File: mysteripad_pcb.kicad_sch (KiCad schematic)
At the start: 74 parts, among them J1 PJ-320A, U1 ATmega328P-PU, Y1 Crystal

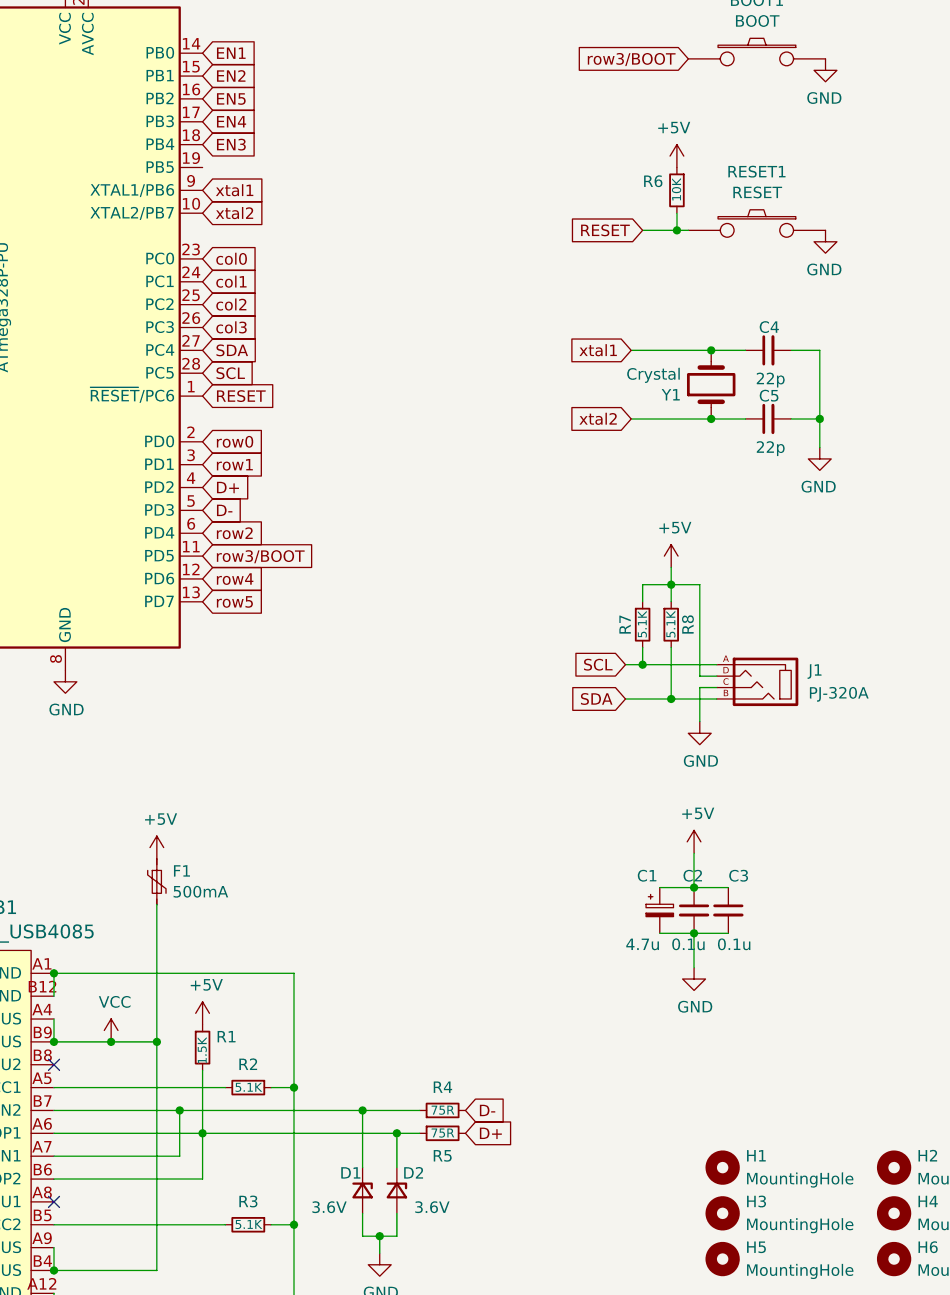
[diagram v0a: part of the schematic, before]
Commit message: Fix incorrect USB pullup; fix bottom mounting holes
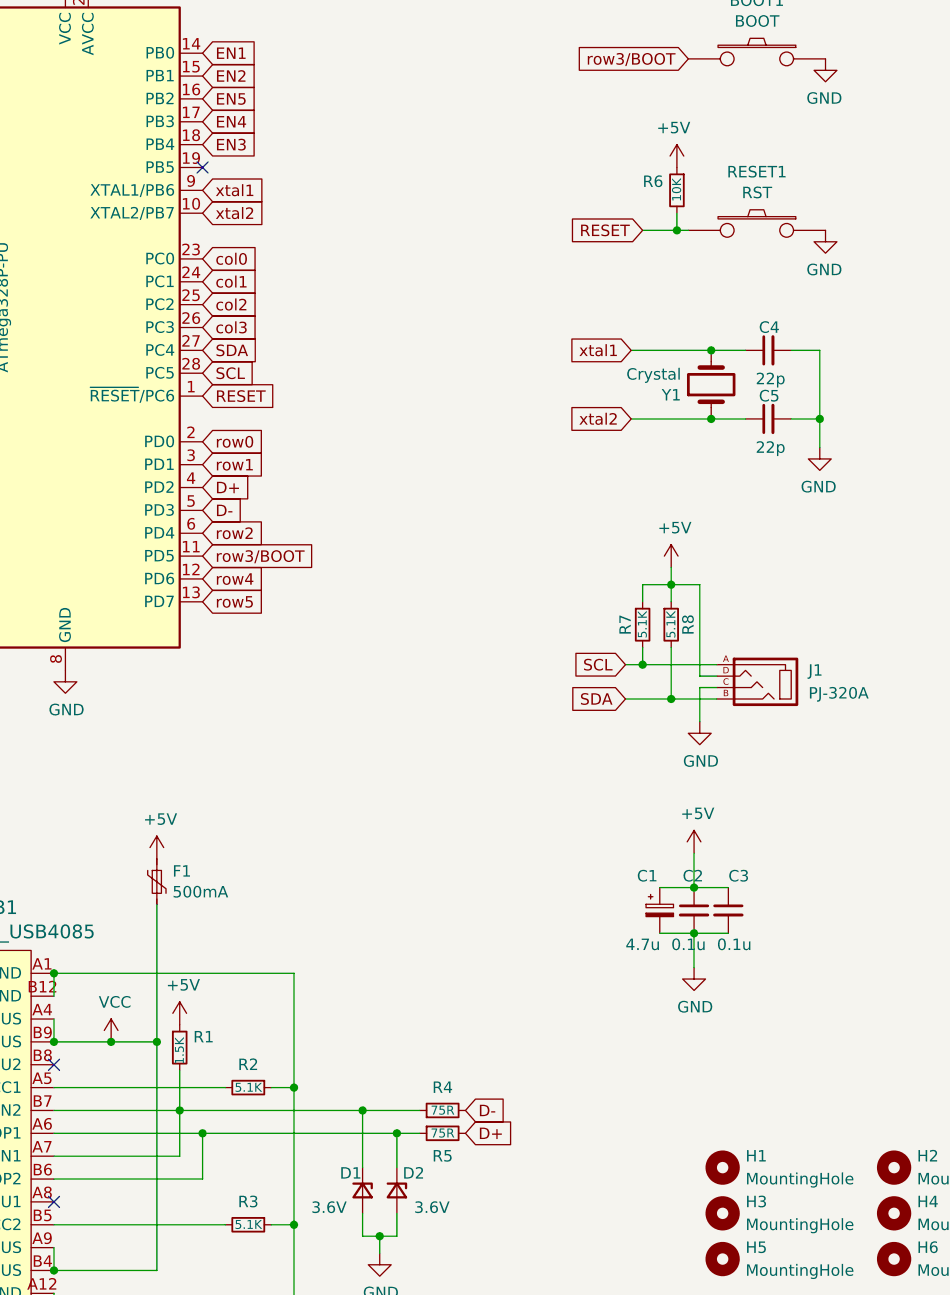
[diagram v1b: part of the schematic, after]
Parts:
- RESET1: value RESET -> RST
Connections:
- net at D2.1 (K), R5.1, USB1.A6 (DP1)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: no longer R1.2
- net at D1.1 (K), R4.1, USB1.A7 (DN1)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: now also R1.2
- no-connect marks 3 -> 4
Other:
- moved on the sheet: R1
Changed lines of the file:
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@@
   )
   (no_connect (at 43.815 163.195))
+  (no_connect (at 60.325 48.26))
   (no_connect (at 29.845 35.56))
   (no_connect (at 43.815 147.955))
@@
     (stroke (width 0) (type default) (color 0 0 0 0))
   )
-  (wire (pts (xy 60.325 148.59) (xy 60.325 155.575))
-    (stroke (width 0) (type default) (color 0 0 0 0))
-  )
   (wire (pts (xy 67.945 150.495) (xy 70.485 150.495))
     (stroke (width 0) (type default) (color 0 0 0 0))
@@
   )
   (wire (pts (xy 107.315 103.505) (xy 109.22 103.505))
+    (stroke (width 0) (type default) (color 0 0 0 0))
+  )
+  (wire (pts (xy 57.785 148.59) (xy 57.785 153.035))
     (stroke (width 0) (type default) (color 0 0 0 0))
   )
@@
     (in_bom yes) (on_board yes)
     (property "Reference" "RESET1" (id 0) (at 121.92 48.768 0))
-    (property "Value" "RESET" (id 1) (at 121.92 51.0794 0))
+    (property "Value" "RST" (id 1) (at 121.92 51.0794 0))
     (property "Footprint" "kbd:ResetSW_1side" (id 2) (at 121.92 55.245 0)
       (effects (font (size 1.524 1.524)) hide)
@@
     (pin "2")
   )
-  (symbol (lib_id "Device:R_Small") (at 60.325 146.05 0) (unit 1)
-    (in_bom yes) (on_board yes)
-    (property "Reference" "R1" (id 0) (at 61.8236 144.8816 0)
-      (effects (font (size 1.27 1.27)) (justify left))
-    )
-    (property "Value" "1.5K" (id 1) (at 60.325 147.955 90)
+  (symbol (lib_id "Device:R_Small") (at 57.785 146.05 0) (unit 1)
+    (in_bom yes) (on_board yes)
+    (property "Reference" "R1" (id 0) (at 59.2836 144.8816 0)
+      (effects (font (size 1.27 1.27)) (justify left))
+    )
+    (property "Value" "1.5K" (id 1) (at 57.785 147.955 90)
       (effects (font (size 0.9906 0.9906)) (justify left))
     )
-    (property "Footprint" "Resistor_THT:R_Axial_DIN0204_L3.6mm_D1.6mm_P5.08mm_Horizontal" (id 2) (at 60.325 146.05 0)
-      (effects (font (size 1.27 1.27)) hide)
-    )
-    (property "Datasheet" "~" (id 3) (at 60.325 146.05 0)
+    (property "Footprint" "Resistor_THT:R_Axial_DIN0204_L3.6mm_D1.6mm_P5.08mm_Horizontal" (id 2) (at 57.785 146.05 0)
+      (effects (font (size 1.27 1.27)) hide)
+    )
+    (property "Datasheet" "~" (id 3) (at 57.785 146.05 0)
       (effects (font (size 1.27 1.27)) hide)
     )
@@
     (pin "2")
   )
-  (symbol (lib_id "power:+5V") (at 60.325 143.51 0) (unit 1)
-    (in_bom yes) (on_board yes)
-    (property "Reference" "#PWR05" (id 0) (at 60.325 147.32 0)
-      (effects (font (size 1.27 1.27)) hide)
-    )
-    (property "Value" "+5V" (id 1) (at 60.706 139.1158 0))
-    (property "Footprint" "" (id 2) (at 60.325 143.51 0)
-      (effects (font (size 1.27 1.27)) hide)
-    )
-    (property "Datasheet" "" (id 3) (at 60.325 143.51 0)
+  (symbol (lib_id "power:+5V") (at 57.785 143.51 0) (unit 1)
+    (in_bom yes) (on_board yes)
+    (property "Reference" "#PWR05" (id 0) (at 57.785 147.32 0)
+      (effects (font (size 1.27 1.27)) hide)
+    )
+    (property "Value" "+5V" (id 1) (at 58.166 139.1158 0))
+    (property "Footprint" "" (id 2) (at 57.785 143.51 0)
+      (effects (font (size 1.27 1.27)) hide)
+    )
+    (property "Datasheet" "" (id 3) (at 57.785 143.51 0)
       (effects (font (size 1.27 1.27)) hide)
     )
@@
     )
     (path "/a1aa8285-04f0-43e3-96ac-17f61afa4f4a"
-      (reference "RESET1") (unit 1) (value "RESET") (footprint "kbd:ResetSW_1side")
+      (reference "RESET1") (unit 1) (value "RST") (footprint "kbd:ResetSW_1side")
     )
     (path "/7e9a60fc-a151-4b1f-a767-423db89d07d4"
